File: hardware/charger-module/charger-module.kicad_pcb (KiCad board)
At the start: 4 copper layers, 80 x 24.3 mm, 74 parts, among them J2 Bus_PCI_Express_x1, J3 RP_USB, J4 USB_C_Receptacle_USB2.0_14P, J5 USB_SW, Q1 2N7002, SW1 RESET, SW2 RESET, U1 AMS1117-3.3, U2 W25Q32JVSSIQ, U3 RP2040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

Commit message: chore: add open hardware logo
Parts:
- added REF**: OSHW-Logo2_9.8x8mm_SilkScreen, Symbol:OSHW-Logo2_9.8x8mm_SilkScreen, B.Cu at (51.0, 40.5)
- moved REF** 0.17 mm to (95.0, 40.5)
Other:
- board text added: "Smart Module ${REVISION}"
- board text removed: "${REVISION}"
- board text removed: "Smart Module"

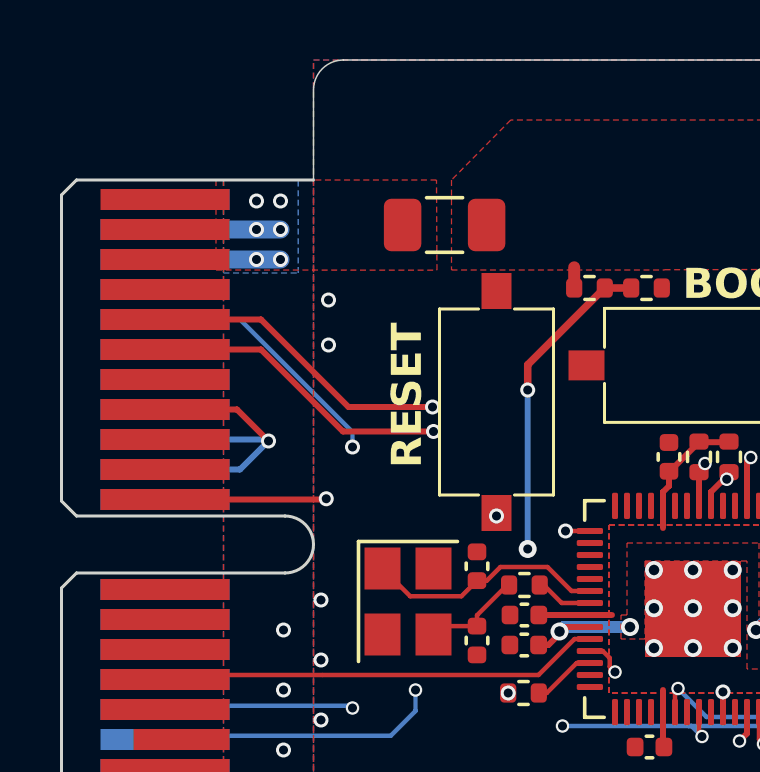
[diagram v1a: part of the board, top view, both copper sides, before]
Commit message: feat: give vin 8 pins
fix: correct i2c pin mismatch
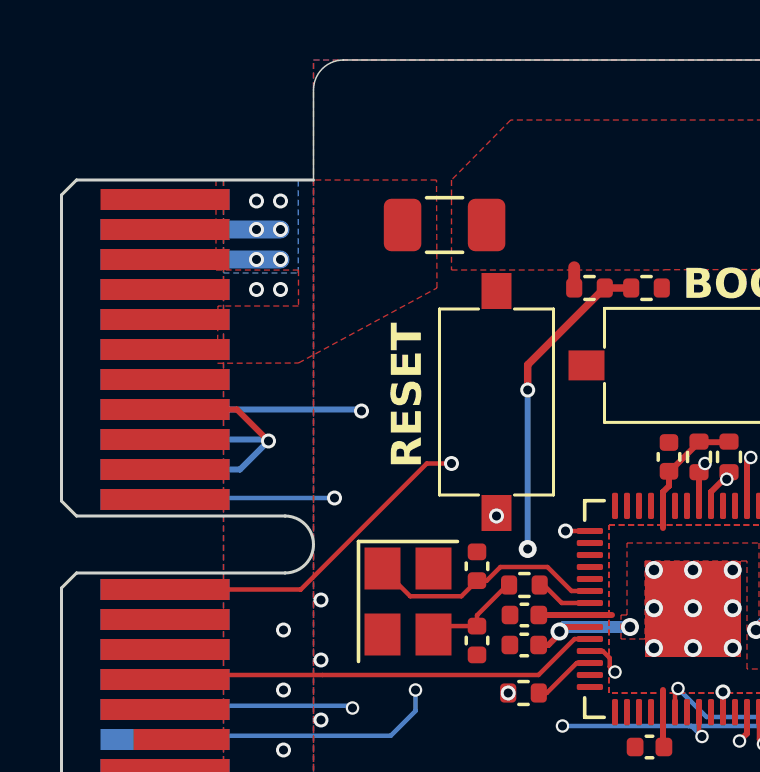
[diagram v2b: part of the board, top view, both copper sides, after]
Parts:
- removed the REF** at (51.0, 40.5)
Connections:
- J2 pad A11: unconnected-(J2-~{PERST}-PadA11) -> /SWD
- J2 pad A5: /SWD -> GND
- J2 pad A6: unconnected-(J2-JTAG3-PadA6) -> GND
- J2 pad A8: unconnected-(J2-JTAG5-PadA8) -> SDA
- J2 pad B12: unconnected-(J2-RSVD-PadB12) -> SCL
- J2 pad B5: SCL -> /VIN_PREFUSE
- J2 pad B6: SDA -> /VIN_PREFUSE
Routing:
- net unconnected-(J2-~{WAKE}-PadB11): track 5.49 -> 0.00 mm, vias 1 -> 0
- net /SWD: track 23.6 -> 21.1 mm
- net SDA: track 81.7 -> 80.9 mm
